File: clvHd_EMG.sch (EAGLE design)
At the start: 25 parts, among them J1 XF2J-1824-12, J2 XF2J-1824-12, U1 ADS1293CISQ/NOPB

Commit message: shrinken
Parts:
- removed J1, J2: XF2J-1824-12, con-omron:XF2J-1824-12
- added 1, 2: X05C2018TZ, con-omron:X05C2018TZ
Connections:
- net A0: now also 1G$3.MS; no longer J1-16.MS
- net A1: now also 1G$5.MS; no longer J1-14.MS
- net A2: now also 1G$6.MS; no longer J1-13.MS
- net A3: now also 1G$8.MS; no longer J1-11.MS
- net CLK: now also 1G$16.MS, 2G$3.MS; no longer J1-3.MS, J2-16.MS
- net DIN: now also 1G$13.MS, 2G$6.MS; no longer J1-6.MS, J2-13.MS
- net DOUT: now also 1G$15.MS, 2G$4.MS; no longer J1-4.MS, J2-15.MS
- net GND: now also 1G$11.MS, 1G$14.MS, 1G$17.MS, 1G$4.MS, 1G$7.MS, 2G$12.MS, 2G$15.MS, 2G$2.MS, 2G$5.MS, 2G$8.MS; no longer J1-12.MS, J1-15.MS, J1-2.MS, J1-5.MS, J1-8.MS, J2-11.MS, J2-14.MS, J2-17.MS, J2-4.MS, J2-7.MS
- net GPIO1: now also 1G$2.MS, 2G$17.MS; no longer J1-17.MS, J2-2.MS
- net IN5: now also 1G$1.MS, 2G$18.MS; no longer J1-18.MS, J2-1.MSV
- net RST: now also 1G$9.MS, 2G$10.MS; no longer J1-10.MS, J2-9.MS
- net S0: now also 2G$16.MS; no longer J2-3.MS
- net S1: now also 2G$14.MS; no longer J2-5.MS
- net S2: now also 2G$13.MS; no longer J2-6.MS
- net S3: now also 2G$11.MS; no longer J2-8.MS
- net SCLK: now also 1G$12.MS, 2G$7.MS; no longer J1-7.MS, J2-12.MS
- net SYNCB: now also 1G$10.MS, 2G$9.MS; no longer J1-9.MS, J2-10.MS
- net VDD: now also 1G$18.MS, 2G$1.MS; no longer J1-1.MSV, J2-18.MS

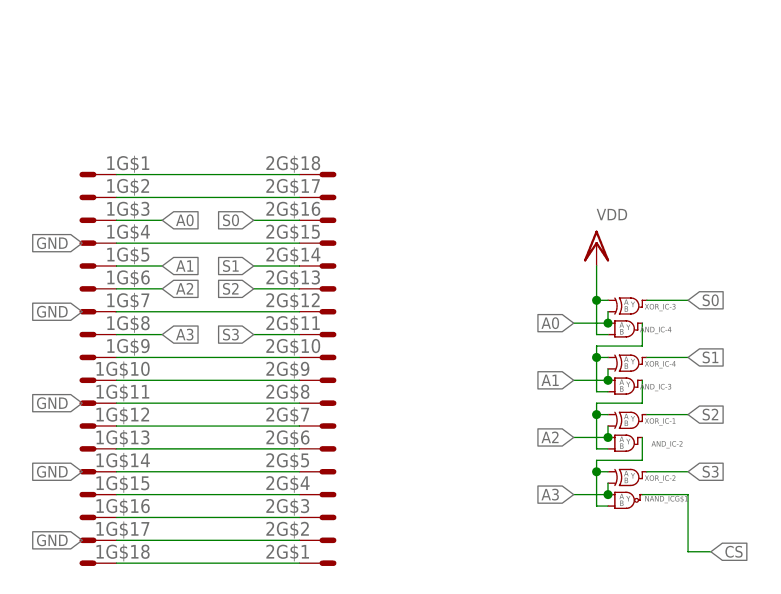
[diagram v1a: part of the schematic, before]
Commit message: dir indication + lvl3 gnd plane
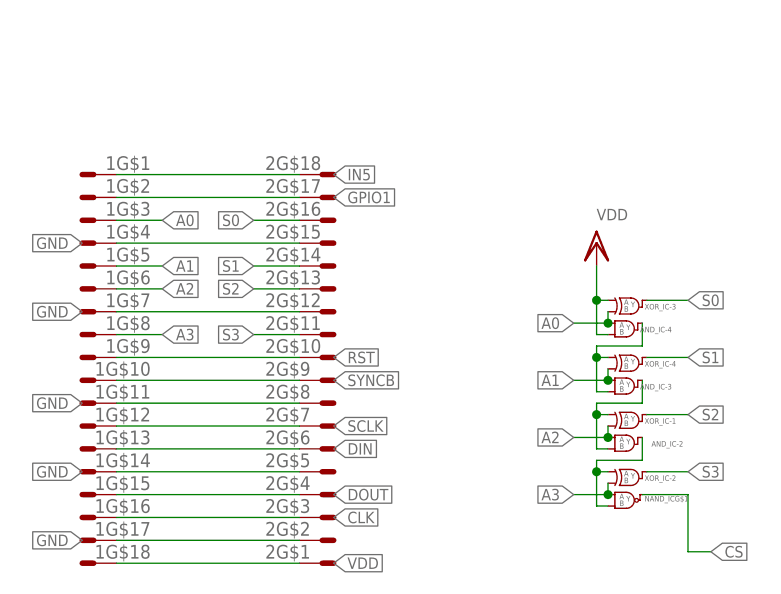
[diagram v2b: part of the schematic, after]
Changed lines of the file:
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@@
 <pinref part="2" gate="G$6" pin="MS"/>
 <pinref part="1" gate="G$13" pin="MS"/>
+<label x="45.72" y="31.75" size="1.27" layer="95" xref="yes" grouprefs="COMMUNICATION"/>
 </segment>
 <segment>
@@
 <pinref part="2" gate="G$4" pin="MS"/>
 <pinref part="1" gate="G$15" pin="MS"/>
+<label x="45.72" y="26.67" size="1.27" layer="95" xref="yes" grouprefs="COMMUNICATION"/>
 </segment>
 <segment>
@@
 <pinref part="2" gate="G$18" pin="MS"/>
 <pinref part="1" gate="G$1" pin="MS"/>
+<label x="45.72" y="62.23" size="1.27" layer="95" xref="yes" grouprefs="COMMUNICATION"/>
 </segment>
 </net>
@@
 <pinref part="2" gate="G$7" pin="MS"/>
 <pinref part="1" gate="G$12" pin="MS"/>
+<label x="45.72" y="34.29" size="1.27" layer="95" xref="yes" grouprefs="COMMUNICATION"/>
 </segment>
 </net>
@@
 <pinref part="2" gate="G$1" pin="MS"/>
 <pinref part="1" gate="G$18" pin="MS"/>
+<label x="45.72" y="19.05" size="1.27" layer="95" xref="yes" grouprefs="COMMUNICATION"/>
 </segment>
 <segment>
@@
 <pinref part="2" gate="G$3" pin="MS"/>
 <pinref part="1" gate="G$16" pin="MS"/>
+<label x="45.72" y="24.13" size="1.27" layer="95" xref="yes" grouprefs="COMMUNICATION"/>
 </segment>
 </net>
@@
 <pinref part="2" gate="G$9" pin="MS"/>
 <pinref part="1" gate="G$10" pin="MS"/>
+<label x="45.72" y="39.37" size="1.27" layer="95" xref="yes" grouprefs="COMMUNICATION"/>
 </segment>
 </net>
@@
 <pinref part="2" gate="G$10" pin="MS"/>
 <pinref part="1" gate="G$9" pin="MS"/>
+<label x="45.72" y="41.91" size="1.27" layer="95" xref="yes" grouprefs="COMMUNICATION"/>
 </segment>
 </net>
@@
 <pinref part="2" gate="G$17" pin="MS"/>
 <pinref part="1" gate="G$2" pin="MS"/>
-</segment>
-</net>
+<label x="45.72" y="59.69" size="1.27" layer="95" xref="yes" grouprefs="COMMUNICATION"/>
+</segment>
+</net>

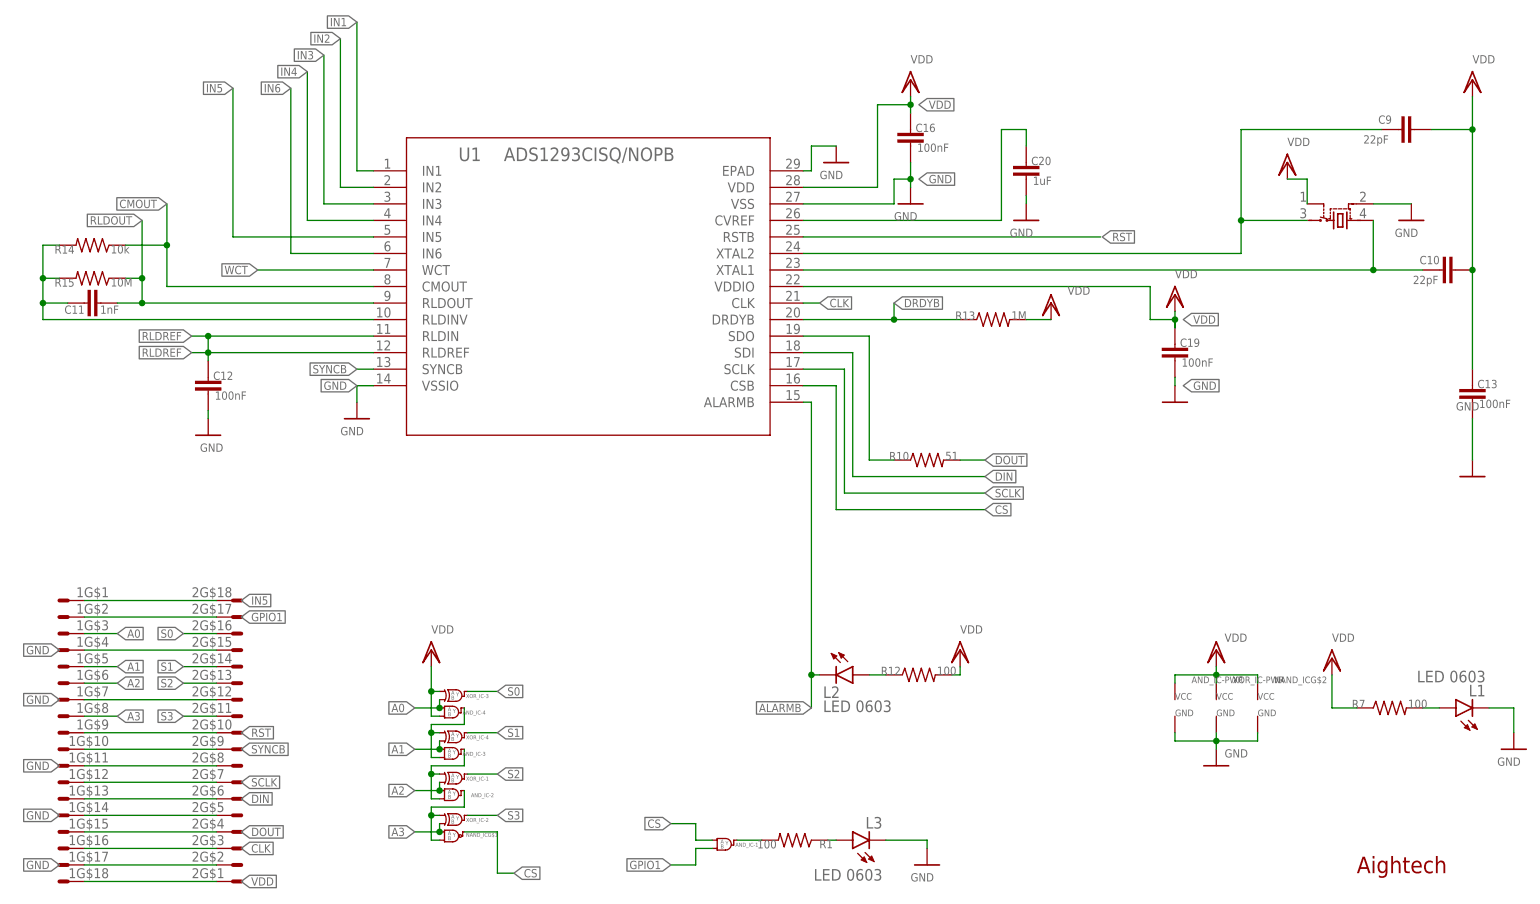
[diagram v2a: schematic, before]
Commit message: double gate nand
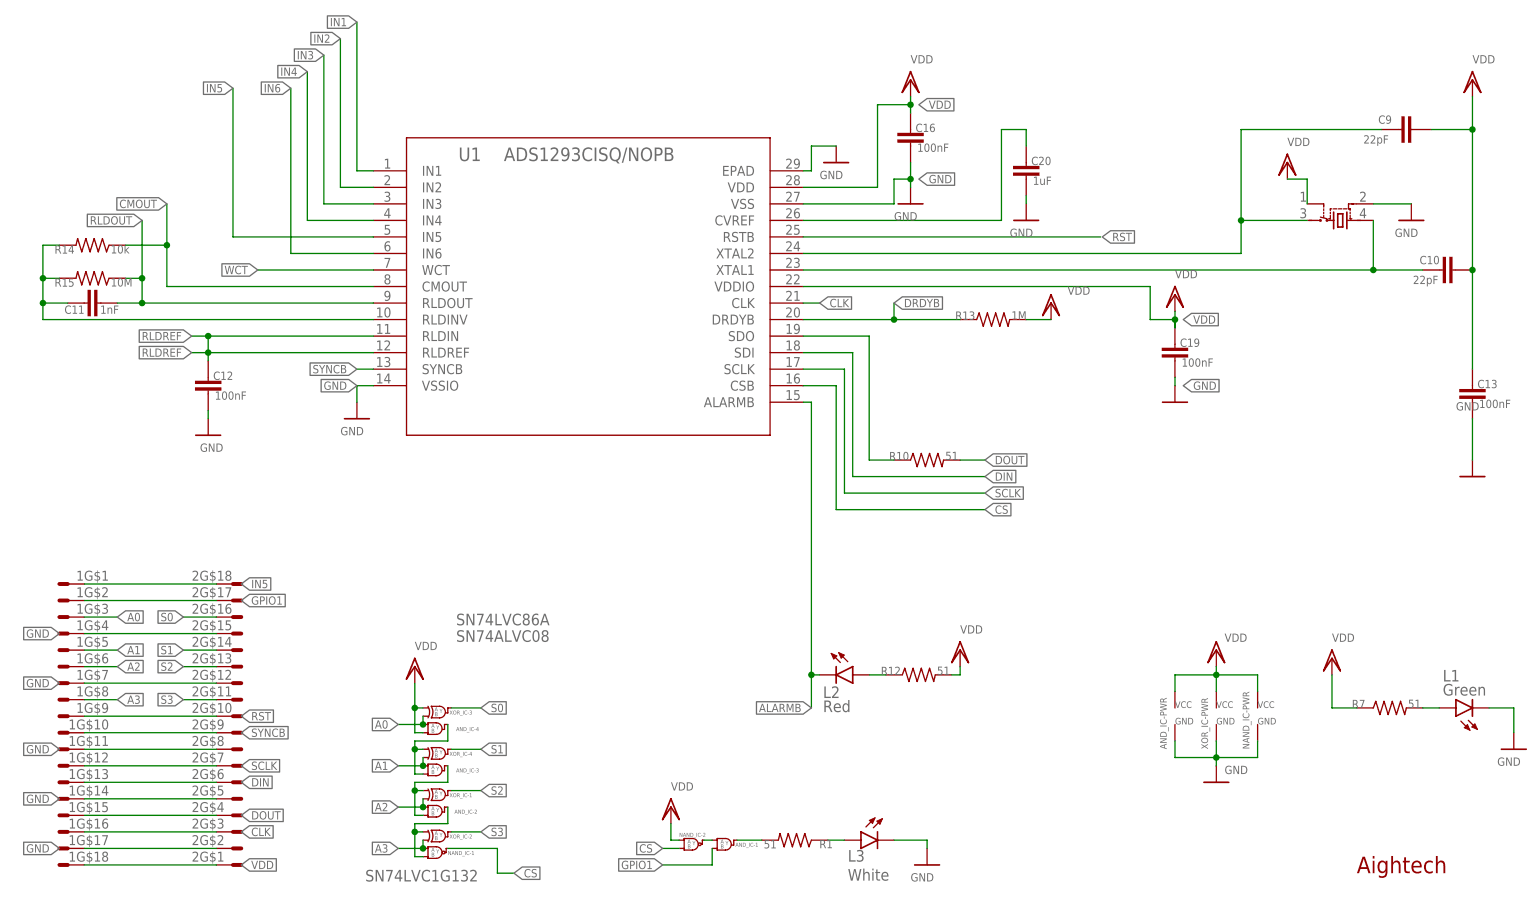
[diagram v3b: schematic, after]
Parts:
- AND_IC: value SN74ALVC08LARGE -> SN74ALVC08RGY-LARGE; device SamacSys_Parts:SN74ALVC08LARGE -> SamacSys_Parts:SN74ALVC08RGY-LARGE
- L1: value LED 0603 -> Green
- L2: value LED 0603 -> Red
- L3: value LED 0603 -> White
- NAND_IC: value SN74LVC1G132DCKT -> SN74AUP2G00YZP; device SamacSys_Parts:SN74LVC1G132DCKT -> SamacSys_Parts:SN74AUP2G00YZP
- R1, R12, R7: value 100 -> 51
- XOR_IC: value SN74LVC86A -> SN74LVC86ARGY-LARGE; device SamacSys_Parts:SN74LVC86A -> SamacSys_Parts:SN74LVC86ARGY-LARGE
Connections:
- new net N$1: AND_IC-1.A, NAND_IC-2.Y
- net A3: now also NAND_IC-1.A; no longer NAND_ICG$1.A
- net CS: now also NAND_IC-1.Y, NAND_IC-2.B; no longer AND_IC-1.A, NAND_ICG$1.Y
- net GND: now also NAND_IC-PWR.GND; no longer NAND_ICG$2.GND
- net N$16: now also NAND_IC-1.B; no longer NAND_ICG$1.B
- net VDD: now also NAND_IC-2.A, NAND_IC-PWR.VCC; no longer NAND_ICG$2.VCC
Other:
- note added: "SN74ALVC08"
- note added: "SN74LVC1G132"
- note added: "SN74LVC86A"
- moved on the sheet: 1G$1, 1G$10, 1G$11, 1G$12, 1G$13, 1G$14, 1G$15, 1G$16, 1G$17, 1G$18, 1G$2, 1G$3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

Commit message: global setup
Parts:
- removed C13, C19: 100nF, rcl:C-EUC0402
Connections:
- net GND: no longer C13.2, C19.2
- net IN5: no longer 1G$1.MS, 2G$18.MS
- net IN6: now also 1G$1.MS, 2G$18.MS
- net VDD: no longer C13.1, C19.1

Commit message: visual mod
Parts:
- removed R15: 10M, rcl:R-US_R0402
- added R2: 51, rcl:R-US_R0402
- ADC: value ADS1293CISQ/NOPB -> ADS1293
- LOGIC_AND: value SN74ALVC08RGY-LARGE -> SN74ALVC08
- LOGIC_NAND: value SN74AUP2G00YZP -> SN74AUP2G00
- LOGIC_XOR: value SN74LVC86ARGY-LARGE -> SN74LVC86
- R7: value 51 -> 10M
- renumbered AND_IC to LOGIC_AND, C10 to C2, C11 to C3, C12 to C5, C16 to C4, C20 to C6, C9 to C1, NAND_IC to LOGIC_NAND, R10 to R3, R12 to R4, R13 to R6, R14 to R5, U$1 to X_TAL, U1 to ADC, XOR_IC to LOGIC_XOR
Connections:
- net N$15: now also R7.2; no longer R15.2
- net N$2: now also R2.2; no longer R7.2
- net RLDOUT: now also R7.1; no longer R15.1
- net VDD: now also R2.1; no longer R7.1
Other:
- moved on the sheet: R7
